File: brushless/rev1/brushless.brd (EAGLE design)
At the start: 30 x 48 mm, 71 parts, among them Q1 BUK7Y12-40E, Q2 BUK7Y12-40E, Q3 BUK7Y12-40E, Q4 BUK7Y12-40E, Q5 BUK7Y12-40E, Q6 BUK7Y12-40E, X2 MOTOR

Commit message: rev1
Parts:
- moved UC1 0.32 mm to (17.8, 13.3)
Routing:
- net GND: track 49.4 -> 246.3 mm, vias 0 -> 4
- net 3.3: track 0.00 -> 95.4 mm, vias 0 -> 5
- net VCC: track 0.00 -> 73.3 mm, vias 0 -> 1
- net V_GATE_HIGH: track 0.00 -> 49.9 mm, vias 0 -> 3
- net VDRIVER: track 0.00 -> 45.3 mm, vias 0 -> 1
- net BUTTON: track 0.00 -> 38.1 mm, vias 0 -> 2
- net V+: track 25.9 -> 63.4 mm, vias 0 -> 1
- net V_LOW: track 0.00 -> 36.6 mm, vias 0 -> 2
- net W_GATE_LOW: track 0.00 -> 35.4 mm, vias 0 -> 1
- net ENC_MISO: track 0.00 -> 34.9 mm, vias 0 -> 2
- net HALLV: track 0.00 -> 32.9 mm, vias 0 -> 2
- net N$22: track 0.00 -> 32.6 mm
- net HALLW: track 0.00 -> 32.2 mm, vias 0 -> 1
- net HALLU: track 0.00 -> 32.1 mm, vias 0 -> 1
- net SCK: track 0.00 -> 31.9 mm, vias 0 -> 1
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
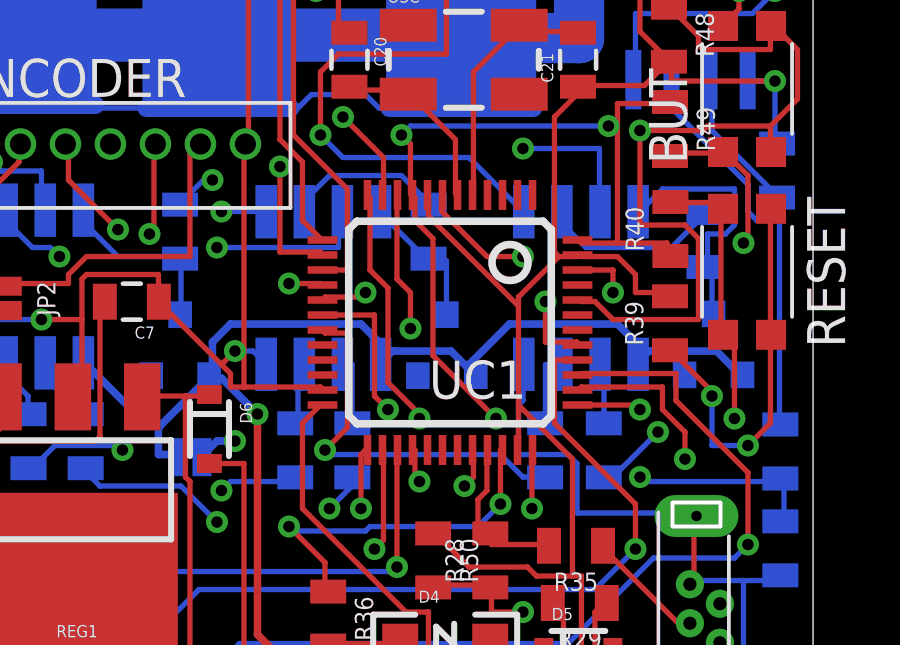
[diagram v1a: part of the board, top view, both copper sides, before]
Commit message: Using 0.25 instead of 0.254 pad width for stm32
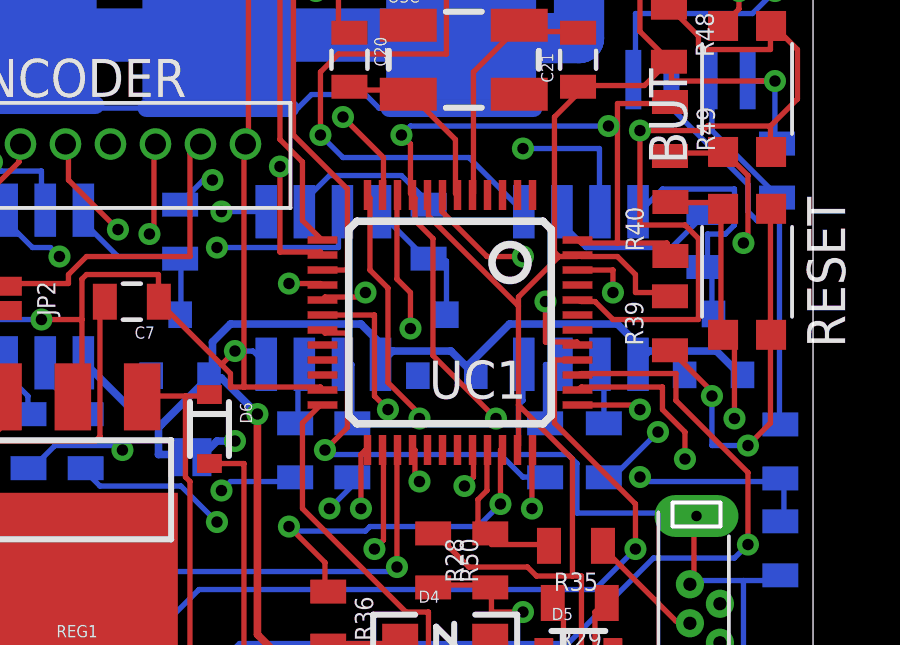
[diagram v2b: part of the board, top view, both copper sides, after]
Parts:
- UC1: device stm32:LQFP48 -> rhoban:STM32_LQFP48
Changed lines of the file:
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@@
 <attribute name="FARNELL" value="1581233" x="17.6578" y="2.5118" size="1.778" layer="27" display="off"/>
 </element>
-<element name="UC1" library="stm32" package="LQFP48" value="STM32F103CBT6" x="17.8182" y="13.251" rot="R180">
+<element name="UC1" library="rhoban" package="STM32_LQFP48" value="STM32F103CBT6" x="17.8182" y="13.251" rot="R180">
 <attribute name="FARNELL" value="1606327" x="17.8182" y="13.251" size="1.778" layer="27" rot="R180" display="off"/>
 </element>
